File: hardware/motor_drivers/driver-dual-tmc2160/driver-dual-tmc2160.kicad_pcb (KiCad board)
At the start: 6 copper layers, 30 x 31 mm, 128 parts, among them J1 XH, J2 XH, Q1 DMT6016, Q10 DMT6016, Q11 DMT6016, Q12 DMT6016, Q13 DMT6016, Q14 DMT6016, Q15 DMT6016, Q16 DMT6016, Q2 DMT6016, Q3 DMT6016, Q4 DMT6016, Q5 DMT6016, Q6 DMT6016, Q7 DMT6016, Q8 DMT6016, Q9 DMT6016, T1 DIAG, T10 CS0, T11 STEP, T12 GND, T13 DIR, T14 EN, T15 STEP, T16 GND, T17 DIAG, T18 DIR, T19 EN, T2 CS0, T3 12V, T4 SCK, T5 GND, T6 SDI, T7 SDO, T8 VCC, T9 Therm, U1 TMC2160, U2 TMC2160

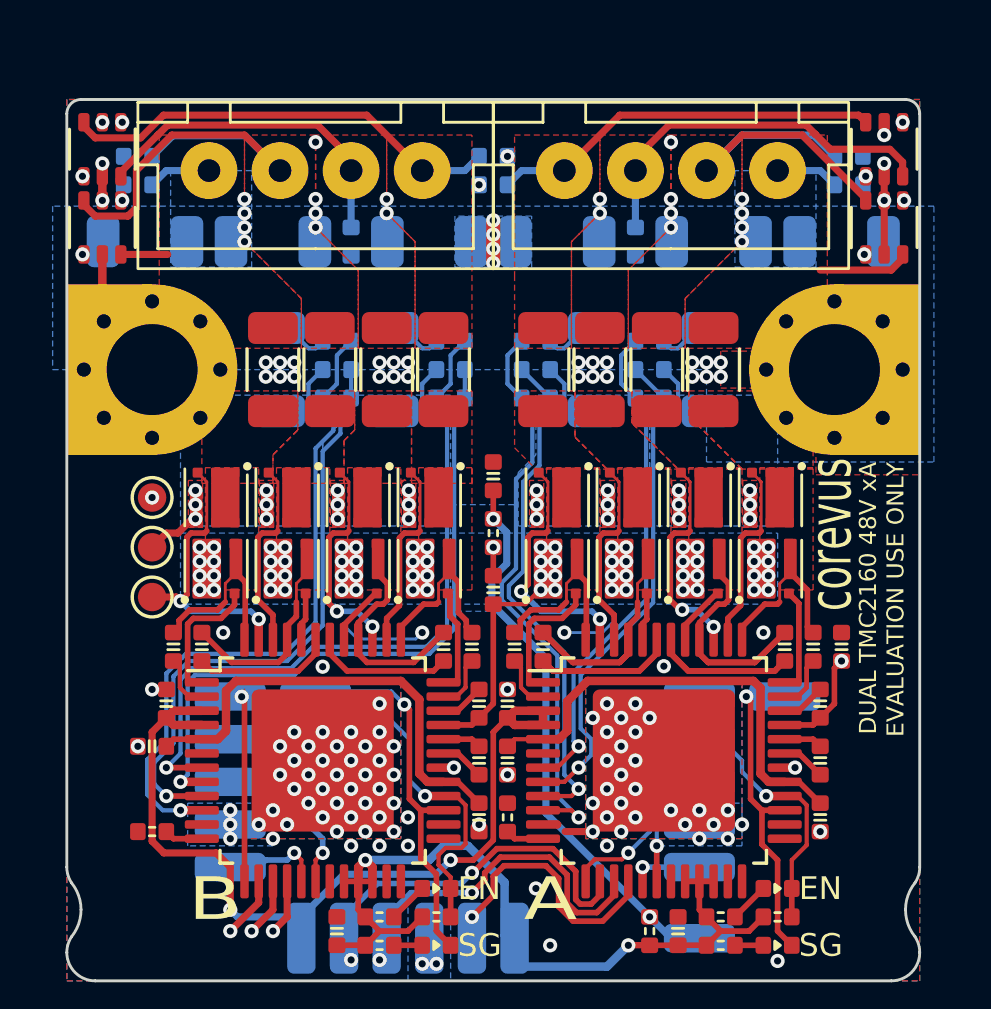
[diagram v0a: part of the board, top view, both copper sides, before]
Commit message: Added STEP and Parasolid mechanical files for Corevus-G v0.6, added TMC2160 + Heater module, added toolboard 4x thermistor expansion, added toolboard MAX31856 thermocouple ADC expansion
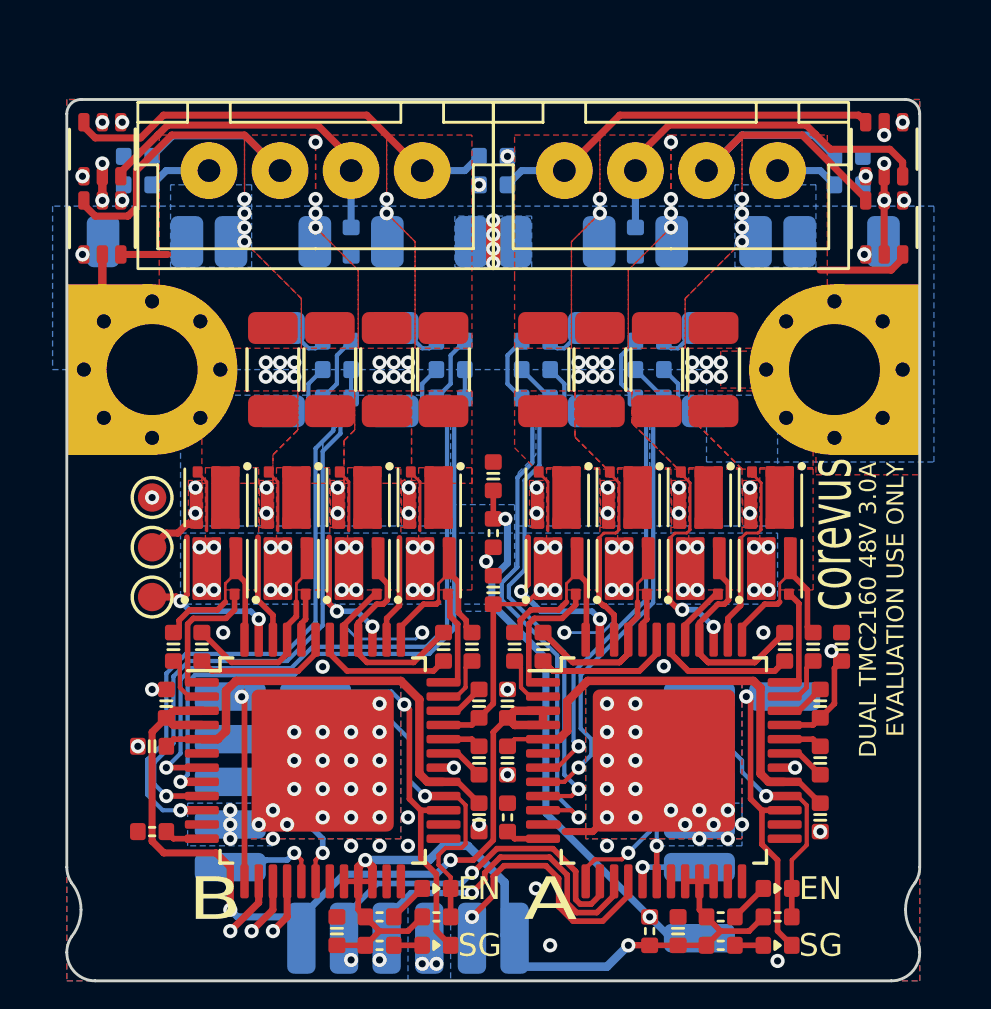
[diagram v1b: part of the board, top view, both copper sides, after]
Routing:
- net GND: track 8.31 -> 7.31 mm, vias 139 -> 113
- net /_{MB}LA2: track 7.23 -> 6.41 mm
- net /_{MB}LA1: track 7.63 -> 6.84 mm
- net /_{MA}LB1: track 8.88 -> 8.09 mm
- net /_{MB}LB2: track 6.80 -> 6.01 mm
- net /_{MB}LB1: track 10.1 -> 9.33 mm
- net +48V: track 19.1 -> 19.6 mm, vias 83 -> 51
- net Net-(Q10-S-Pad4): track 3.15 -> 3.17 mm, vias 6 -> 4
- net Net-(Q6-S-Pad4): vias 6 -> 4
- net Net-(Q2-S-Pad4): vias 6 -> 4
- net Net-(Q14-S-Pad4): vias 6 -> 4
- removed copper zone on In3.Cu, net +48V
- removed copper zone on In3.Cu, net GND
- removed copper zone on In4.Cu, net GND
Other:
- copper layers 6 -> 4
- board text added: "DUAL TMC2160 48V 3.0A EVALUATION USE ONLY"
- board text added: "MERIDI ENGINEERING AUGUST 2024 DUAL TMC2160 STEPPER DRIVER MODULE 48V MAX 3.0A(rms) MAX PER DRIVER"
- board text removed: "DUAL TMC2160 48V xA EVALUATION USE ONLY"
- board text removed: "NOT FOR PRODUCTION USE MERIDI ENGINEERING JULY 2024 DUAL TMC2160 STEPPER DRIVER MODULE 48V MAX xArms MAX PER DRIVER"

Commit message: update toolboard, change documentation
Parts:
- removed H4: ToolingHole, corevus:ToolingHole
- removed TP6: TestPoint, TestPoint:TestPoint_Pad_D1.0mm
- added C42: 100nF 100V, PCM_ME_passives:0402C, B.Cu at (134.8, 70.8)
- added C43: 100nF 100V, PCM_ME_passives:0402C, B.Cu at (135.8, 70.8)
- added C44: 100nF 100V, PCM_ME_passives:0402C, B.Cu at (136.8, 70.7)
- added C45: 100nF 100V, PCM_ME_passives:0402C, B.Cu at (146.8, 69.8)
- added C46: 100nF 100V, PCM_ME_passives:0402C, B.Cu at (146.8, 68.8)
- added C47: 100nF 100V, PCM_ME_passives:0402C, B.Cu at (146.8, 67.8)
- added C48: 100nF 100V, PCM_ME_passives:0402C, B.Cu at (146.8, 66.8)
- added C49: 100nF 100V, PCM_ME_passives:0402C, B.Cu at (146.8, 65.8)
- added C50: 100nF 100V, PCM_ME_passives:0402C, B.Cu at (146.8, 64.8)
- added FID1: Fiducial, Fiducial:Fiducial_0.5mm_Mask1mm, F.Cu at (121.5, 64.5)
- added FID2: Fiducial, Fiducial:Fiducial_0.5mm_Mask1mm, F.Cu at (136.0, 78.5)
- added FID3: Fiducial, Fiducial:Fiducial_0.5mm_Mask1mm, B.Cu at (122.5, 73.2)
- added FID4: Fiducial, Fiducial:Fiducial_0.5mm_Mask1mm, B.Cu at (145.5, 64.0)
- added NT5: NetTie_2, corevus:NetTie-2_SMD_Pad0.15mm, B.Cu at (129.2, 61.1)
- added NT6: NetTie_2, corevus:NetTie-2_SMD_Pad0.15mm, B.Cu at (129.2, 58.5)
- added NT7: NetTie_2, corevus:NetTie-2_SMD_Pad0.15mm, B.Cu at (131.8, 61.1)
- added NT8: NetTie_2, corevus:NetTie-2_SMD_Pad0.15mm, B.Cu at (131.8, 58.5)
- added REF**: BackScrew, corevus:BackScrew, F.Cu at (151.0, 79.0)
- added REF**: BackScrew, corevus:BackScrew, F.Cu at (119.0, 79.0)
- C13, C28, TH1: moved to B.Cu
- C20, C21, C33, C41: value 1nF -> 1nF
- D1, D2, D5, D6: footprint PCM_ME_passives:0402LED -> PCM_ME_passives:0603LED
- H1, H2: footprint corevus:MountingHole_M3_Driver -> corevus:MountingHole_M3_Driver_1
- NT1, NT2, NT3, NT4: footprint corevus:NetTie-2_SMD_Pad0.1mm -> corevus:NetTie-2_SMD_Pad0.15mm
- moved NT3 12.8 mm to (140.8, 61.1), turned to 180 degrees
- moved NT4 8.60 mm to (140.8, 58.5), turned to 180 degrees
- moved TP1 4.28 mm to (122.5, 68.8)
- moved NT2 3.62 mm to (138.2, 58.5), turned to 180 degrees
- moved R19 3.30 mm to (131.0, 62.1), turned to 90 degrees
- moved R8 3.30 mm to (139.0, 62.1), turned to 90 degrees
- moved C28 3.25 mm to (133.8, 70.8), turned to -90 degrees
- moved C20 2.58 mm to (139.0, 60.4), turned to -90 degrees
- moved C41 2.58 mm to (131.0, 60.4), turned to -90 degrees
- moved D5 2.55 mm to (133.5, 80.8)
- moved D1 2.55 mm to (145.5, 80.8)
- moved R21 2.54 mm to (131.0, 58.5), turned to -90 degrees
- moved R9 2.54 mm to (139.0, 58.5), turned to -90 degrees
- moved NT1 2.26 mm to (138.2, 61.1), turned to 180 degrees
- moved R11 2.21 mm to (140.0, 62.1), turned to 90 degrees
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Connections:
- NT1 pad 2: GND -> Net-(NT1-Pad2)
- NT2 pad 1: GND -> Net-(NT2-Pad1)
- NT2 pad 2: Net-(NT2-Pad2) -> GND
- NT3 pad 2: GND -> Net-(NT3-Pad2)
- Q10 pad 4: Net-(Q10-S-Pad4) -> Net-(NT5-Pad2)
- Q10 pad 7: Net-(Q10-S-Pad4) -> Net-(NT5-Pad2)
- Q12 pad 4: Net-(Q10-S-Pad4) -> Net-(NT5-Pad2)
- Q12 pad 7: Net-(Q10-S-Pad4) -> Net-(NT5-Pad2)
- Q14 pad 4: Net-(Q14-S-Pad4) -> Net-(NT7-Pad1)
- Q14 pad 7: Net-(Q14-S-Pad4) -> Net-(NT7-Pad1)
- Q16 pad 4: Net-(Q14-S-Pad4) -> Net-(NT7-Pad1)
- Q16 pad 7: Net-(Q14-S-Pad4) -> Net-(NT7-Pad1)
- Q2 pad 4: Net-(Q2-S-Pad4) -> Net-(NT1-Pad2)
- Q2 pad 7: Net-(Q2-S-Pad4) -> Net-(NT1-Pad2)
- Q4 pad 4: Net-(Q2-S-Pad4) -> Net-(NT1-Pad2)
- Q4 pad 7: Net-(Q2-S-Pad4) -> Net-(NT1-Pad2)
- Q6 pad 4: Net-(Q6-S-Pad4) -> Net-(NT3-Pad1)
- Q6 pad 7: Net-(Q6-S-Pad4) -> Net-(NT3-Pad1)
- Q8 pad 4: Net-(Q6-S-Pad4) -> Net-(NT3-Pad1)
- Q8 pad 7: Net-(Q6-S-Pad4) -> Net-(NT3-Pad1)
- R10 pad 1: Net-(Q2-S-Pad4) -> Net-(NT1-Pad2)
- R11 pad 1: Net-(Q6-S-Pad4) -> Net-(NT3-Pad2)
- R12 pad 1: Net-(NT2-Pad2) -> Net-(NT4-Pad2)
- R13 pad 1: Net-(Q6-S-Pad4) -> Net-(NT3-Pad1)
- R14 pad 1: Net-(Q10-S-Pad4) -> Net-(NT5-Pad1)
- R15 pad 1: Net-(NT3-Pad1) -> Net-(NT6-Pad1)
- R17 pad 1: Net-(Q10-S-Pad4) -> Net-(NT5-Pad2)
- R18 pad 1: Net-(Q14-S-Pad4) -> Net-(NT7-Pad1)
- R19 pad 1: Net-(Q14-S-Pad4) -> Net-(NT7-Pad2)
- R21 pad 1: Net-(NT4-Pad2) -> Net-(NT8-Pad2)
- R8 pad 1: Net-(Q2-S-Pad4) -> Net-(NT1-Pad1)
- R9 pad 1: Net-(NT1-Pad1) -> Net-(NT2-Pad1)
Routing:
- net GND: track 7.31 -> 69.9 mm, vias 113 -> 268
- net /_{MB}SRAL: track 25.3 -> 19.4 mm, vias 1 -> 2
- net /_{MA}A1: track 11.5 -> 5.58 mm
- net Net-(U1-CB2): track 9.78 -> 4.40 mm
- net Net-(U1-CA1): track 9.78 -> 4.40 mm
- net +12V: track 31.1 -> 36.4 mm, vias 2 -> 3
- net VCC: track 29.7 -> 34.8 mm, vias 2 -> 4
- net /_{MA}SRBH: track 18.1 -> 23.1 mm, vias 1 -> 2
- net /_{MA}~{En}: track 8.30 -> 12.9 mm
- net /THERM: track 19.7 -> 24.2 mm
- net /_{MB}~{CS}: track 6.53 -> 10.1 mm
- net /SDI: track 18.4 -> 21.6 mm, vias 3 -> 2
- net Net-(Q10-S-Pad4): track 3.17 -> 0.00 mm, vias 4 -> 0
- net /_{MB}SRAH: track 23.8 -> 20.8 mm, vias 1 -> 2
- net /_{MB}B1: track 6.08 -> 3.62 mm
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- added copper zone on F.Cu, net +48V
- added copper zone on B.Cu, net Net-(NT1-Pad2)
- added copper zone on F.Cu, net Net-(NT1-Pad2)
- added copper zone on B.Cu, net Net-(NT3-Pad1)
- added copper zone on F.Cu, net Net-(NT3-Pad1)
- added copper zone on B.Cu, net Net-(NT5-Pad2)
- added copper zone on F.Cu, net Net-(NT5-Pad2)
- added copper zone on B.Cu, net Net-(NT7-Pad1)
- added copper zone on F.Cu, net Net-(NT7-Pad1)
- removed copper zone on B.Cu, net Net-(Q10-S-Pad4)
- removed copper zone on F.Cu, net Net-(Q10-S-Pad4)
- removed copper zone on B.Cu, net Net-(Q14-S-Pad4)
- removed copper zone on F.Cu, net Net-(Q14-S-Pad4)
- removed copper zone on B.Cu, net Net-(Q2-S-Pad4)
- removed copper zone on F.Cu, net Net-(Q2-S-Pad4)
- removed copper zone on B.Cu, net Net-(Q6-S-Pad4)
- removed copper zone on F.Cu, net Net-(Q6-S-Pad4)
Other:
- board size 30 x 31 mm -> 30 x 32 mm
- board text added: "DUAL TMC2160 48V 3.0A"
- board text added: "E"
- board text added: "MERIDI ENGINEERING DEC 2024 DUAL TMC2160 STEPPER DRIVER MODULE 48V MAX 3.0A MAX PER DRIVER"
- board text added: "S"
- board text removed: "DUAL TMC2160 48V 3.0A EVALUATION USE ONLY"
- board text removed: "MERIDI ENGINEERING AUGUST 2024 DUAL TMC2160 STEPPER DRIVER MODULE 48V MAX 3.0A(rms) MAX PER DRIVER"
- board text removed: "SG"
